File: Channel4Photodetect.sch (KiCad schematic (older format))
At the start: 5 parts

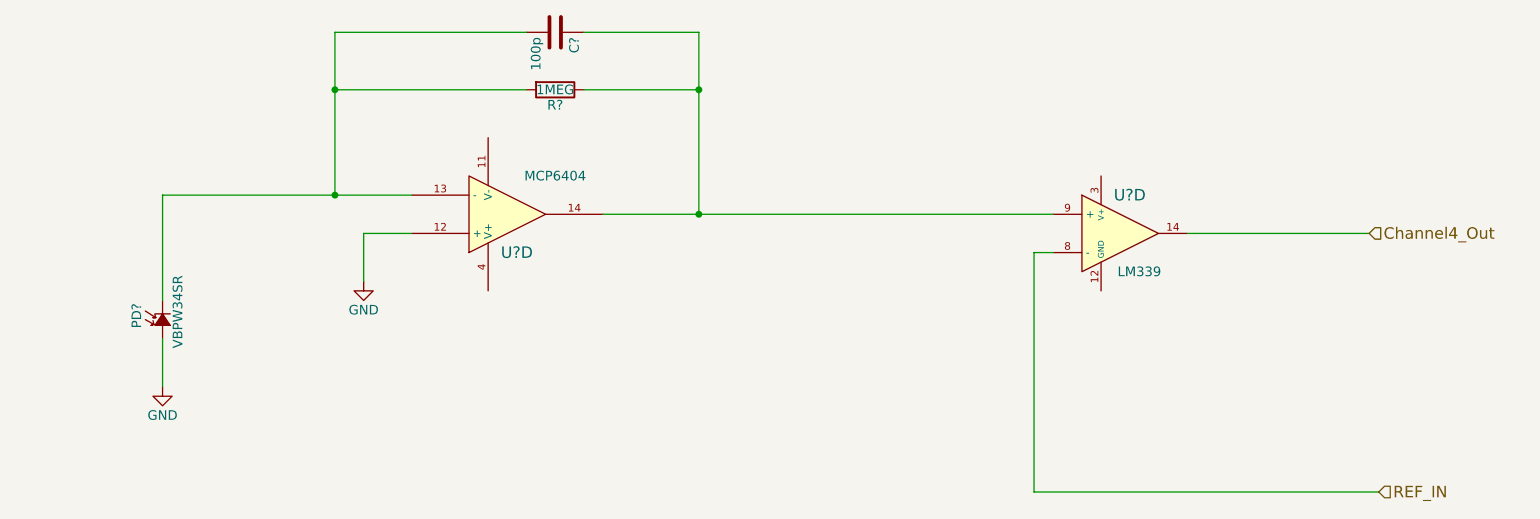
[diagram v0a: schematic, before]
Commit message: Added power regulator, VGND and test points
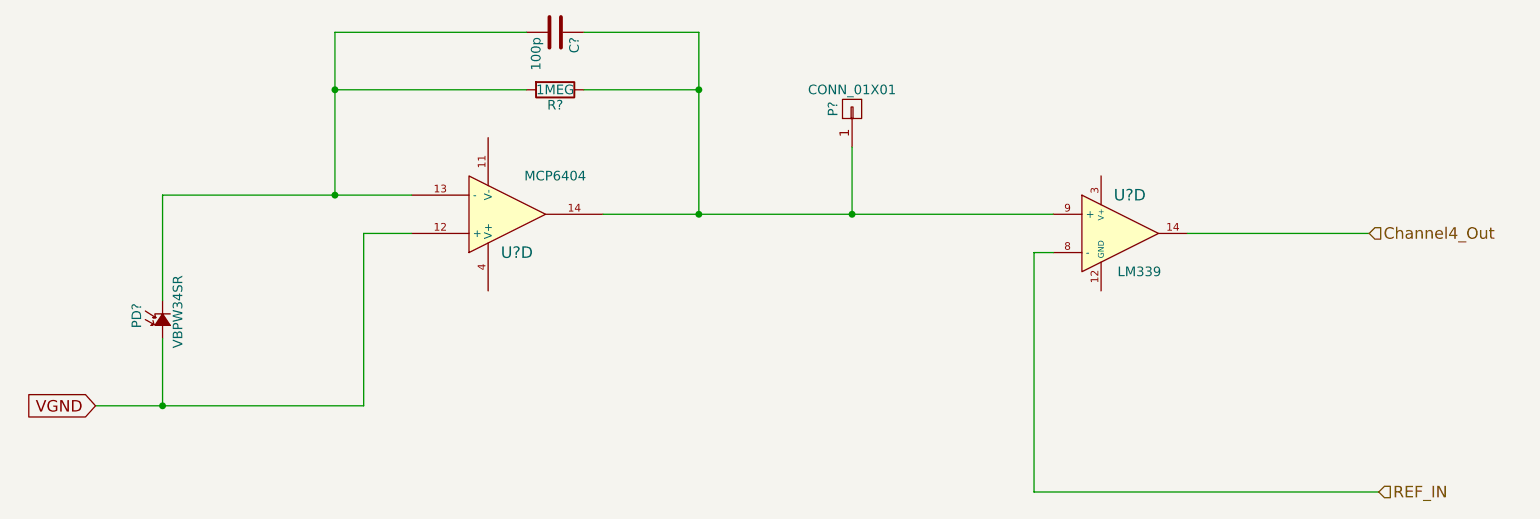
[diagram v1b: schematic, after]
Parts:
- added P?: CONN_01X01, symbol CONN_01X01
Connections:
- net at C?.1, R?.1, U?.14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: now also P?.1 (P1)
- net GND renamed VGND
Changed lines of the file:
@@
 LIBS:memory
 LIBS:xilinx
-LIBS:special
 LIBS:microcontrollers
 LIBS:dsp
@@
 	4550 2550 5150 2550
 Connection ~ 5150 2850
-$Comp
-L GND #PWR?
-U 1 1 5552FFE1
-P 3400 3850
-F 0 "#PWR?" H 3400 3600 50  0001 C CNN
-F 1 "GND" H 3400 3700 50  0000 C CNN
-F 2 "" H 3400 3850 60  0000 C CNN
-F 3 "" H 3400 3850 60  0000 C CNN
-	1    3400 3850
-	1    0    0    -1
-$EndComp
 Wire Wire Line
 	3650 3600 3400 3600
-Wire Wire Line
-	3400 3600 3400 3850
-$Comp
-L GND #PWR?
-U 1 1 5552FFFC
-P 2350 4400
-F 0 "#PWR?" H 2350 4150 50  0001 C CNN
-F 1 "GND" H 2350 4250 50  0000 C CNN
-F 2 "" H 2350 4400 60  0000 C CNN
-F 3 "" H 2350 4400 60  0000 C CNN
-	1    2350 4400
-	1    0    0    -1
-$EndComp
-Wire Wire Line
-	2350 4150 2350 4400
 $Comp
 L LM339 U?
@@
 Wire Wire Line
 	6900 4950 6900 3700
+$Comp
+L CONN_01X01 P?
+U 1 1 555633D1
+P 5950 2950
+F 0 "P?" H 5950 3050 50  0000 C CNN
+F 1 "CONN_01X01" V 6050 2950 50  0000 C CNN
+F 2 "" H 5950 2950 60  0000 C CNN
+F 3 "" H 5950 2950 60  0000 C CNN
+	1    5950 2950
+	0    -1   -1   0
+$EndComp
+Wire Wire Line
+	5950 3150 5950 3500
+Connection ~ 5950 3500
+Wire Wire Line
+	3400 4500 3400 3600
+Wire Wire Line
+	2000 4500 3400 4500
+Wire Wire Line
+	2350 4500 2350 4150
+Text GLabel 2000 4500 0    60   Input ~ 0
+VGND
+Connection ~ 2350 4500
 $EndSCHEMATC

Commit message: Added libraries and imported components into the layout
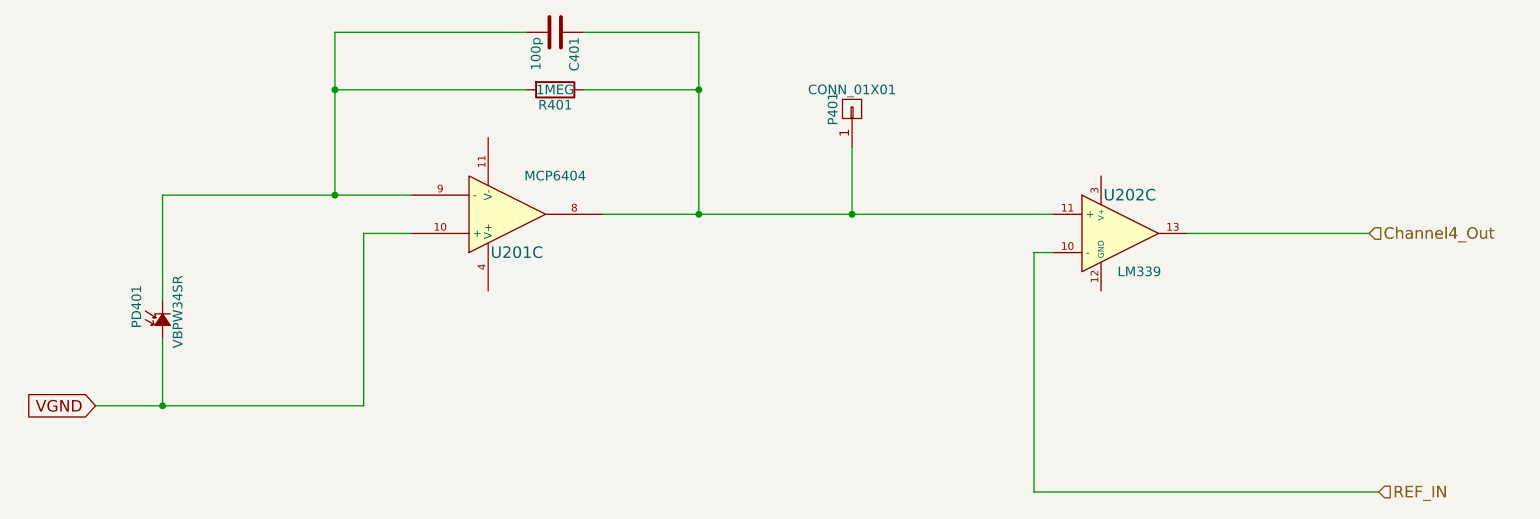
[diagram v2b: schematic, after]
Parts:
- gave numbers to parts that had none: 6
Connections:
- net Channel4_Out: now also U202.13; no longer U202.14
- net REF_IN: now also U202.10 (-); no longer U202.8 (-)
- net VGND: now also U201.10 (+); no longer U201.12 (+)
- net at C401.1, P401.1 (P1), R401.1: now also U201.8, U202.11 (+); no longer U201.14, U202.9 (+)
- net at C401.2, PD401.2 (C), R401.2: now also U201.9 (-); no longer U201.13 (-)
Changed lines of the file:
@@
 $EndDescr
 $Comp
-L R R?
+L R R401
 U 1 1 5552FFAC
 P 4400 2850
-F 0 "R?" V 4480 2850 50  0000 C CNN
+F 0 "R401" V 4480 2850 50  0000 C CNN
 F 1 "1MEG" V 4400 2850 50  0000 C CNN
 F 2 "" V 4330 2850 30  0000 C CNN
@@
 $EndComp
 $Comp
-L C C?
+L C C401
 U 1 1 5552FFB3
 P 4400 2550
-F 0 "C?" H 4425 2650 50  0000 L CNN
+F 0 "C401" H 4425 2650 50  0000 L CNN
 F 1 "100p" H 4425 2450 50  0000 L CNN
 F 2 "" H 4438 2400 30  0000 C CNN
@@
 $EndComp
 $Comp
-L MCP6404-E/SL U?
-U 4 1 5552FFBC
+L MCP6404-E/SL U201
+U 3 1 5552FFBC
 P 4150 3500
-F 0 "U?" H 4200 3700 60  0000 C CNN
+F 0 "U201" H 4200 3700 60  0000 C CNN
 F 1 "MCP6404" H 4400 3300 50  0000 C CNN
 F 2 "" H 4150 3500 60  0000 C CNN
@@
 F 4 "MCP6404-E/SL" H 4150 3500 60  0001 C CNN "MPN"
 F 5 "http://parts.io/detail/3584122/MCP6404-E%2FSL" H 4150 3500 60  0001 C CNN "Link"
-	4    4150 3500
+	3    4150 3500
 	1    0    0    1
 $EndComp
 $Comp
-L Photodiode PD?
+L Photodiode PD401
 U 1 1 5552FFC5
 P 2350 4050
-F 0 "PD?" H 2305 4185 50  0000 L CNN
+F 0 "PD401" H 2305 4185 50  0000 L CNN
 F 1 "VBPW34SR" H 2200 3970 50  0000 L CNN
 F 2 "" V 2350 4050 60  0000 C CNN
@@
 	3650 3600 3400 3600
 $Comp
-L LM339 U?
-U 4 1 55530005
+L LM339 U202
+U 3 1 55530005
 P 7350 3600
-F 0 "U?" H 7400 3800 60  0000 C CNN
+F 0 "U202" H 7400 3800 60  0000 C CNN
 F 1 "LM339" H 7450 3400 50  0000 C CNN
 F 2 "" H 7350 3600 60  0000 C CNN
@@
 F 4 "LM339DE4" H 7350 3600 60  0001 C CNN "MPN"
 F 5 "http://parts.io/detail/916254/LM339DE4" H 7350 3600 60  0001 C CNN "Link"
-	4    7350 3600
+	3    7350 3600
 	1    0    0    -1
 $EndComp
@@
 	6900 4950 6900 3700
 $Comp
-L CONN_01X01 P?
+L CONN_01X01 P401
 U 1 1 555633D1
 P 5950 2950
-F 0 "P?" H 5950 3050 50  0000 C CNN
+F 0 "P401" H 5950 3050 50  0000 C CNN
 F 1 "CONN_01X01" V 6050 2950 50  0000 C CNN
 F 2 "" H 5950 2950 60  0000 C CNN
@@
 Connection ~ 5950 3500
 Wire Wire Line
-	3400 4500 3400 3600
+	3400 3600 3400 4500
 Wire Wire Line
-	2000 4500 3400 4500
+	3400 4500 2000 4500
 Wire Wire Line
 	2350 4500 2350 4150

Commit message: Added photodiode component to new local footprint library
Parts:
- C401: footprint (none) -> Capacitors_SMD:C_0805_HandSoldering
- P401: footprint (none) -> Pin_Headers:Pin_Header_Straight_1x01
- PD401: footprint (none) -> DasBlinkinput:VPW34SR
- R401: footprint (none) -> Resistors_SMD:R_1206_HandSoldering
- U201, U202: footprint (none) -> Housings_SOIC:SOIC-14_3.9x8.7mm_Pitch1.27mm
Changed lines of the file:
@@
 F 0 "R401" V 4480 2850 50  0000 C CNN
 F 1 "1MEG" V 4400 2850 50  0000 C CNN
-F 2 "" V 4330 2850 30  0000 C CNN
+F 2 "Resistors_SMD:R_1206_HandSoldering" V 4330 2850 30  0001 C CNN
 F 3 "" H 4400 2850 30  0000 C CNN
 F 4 "RC1206FR-071ML" V 4400 2850 60  0001 C CNN "MPN"
@@
 F 0 "C401" H 4425 2650 50  0000 L CNN
 F 1 "100p" H 4425 2450 50  0000 L CNN
-F 2 "" H 4438 2400 30  0000 C CNN
+F 2 "Capacitors_SMD:C_0805_HandSoldering" H 4438 2400 30  0001 C CNN
 F 3 "" H 4400 2550 60  0000 C CNN
 	1    4400 2550
@@
 F 0 "U201" H 4200 3700 60  0000 C CNN
 F 1 "MCP6404" H 4400 3300 50  0000 C CNN
-F 2 "" H 4150 3500 60  0000 C CNN
+F 2 "Housings_SOIC:SOIC-14_3.9x8.7mm_Pitch1.27mm" H 4150 3500 60  0001 C CNN
 F 3 "" H 4150 3500 60  0000 C CNN
 F 4 "MCP6404-E/SL" H 4150 3500 60  0001 C CNN "MPN"
@@
 F 0 "PD401" H 2305 4185 50  0000 L CNN
 F 1 "VBPW34SR" H 2200 3970 50  0000 L CNN
-F 2 "" V 2350 4050 60  0000 C CNN
+F 2 "DasBlinkinput:VPW34SR" V 2350 4050 60  0001 C CNN
 F 3 "" V 2350 4050 60  0000 C CNN
 F 4 "VBPW34SR" H 2350 4050 60  0001 C CNN "MPN"
@@
 F 0 "U202" H 7400 3800 60  0000 C CNN
 F 1 "LM339" H 7450 3400 50  0000 C CNN
-F 2 "" H 7350 3600 60  0000 C CNN
+F 2 "Housings_SOIC:SOIC-14_3.9x8.7mm_Pitch1.27mm" H 7350 3600 60  0001 C CNN
 F 3 "" H 7350 3600 60  0000 C CNN
 F 4 "LM339DE4" H 7350 3600 60  0001 C CNN "MPN"
@@
 F 0 "P401" H 5950 3050 50  0000 C CNN
 F 1 "CONN_01X01" V 6050 2950 50  0000 C CNN
-F 2 "" H 5950 2950 60  0000 C CNN
+F 2 "Pin_Headers:Pin_Header_Straight_1x01" H 5950 2950 60  0001 C CNN
 F 3 "" H 5950 2950 60  0000 C CNN
 	1    5950 2950

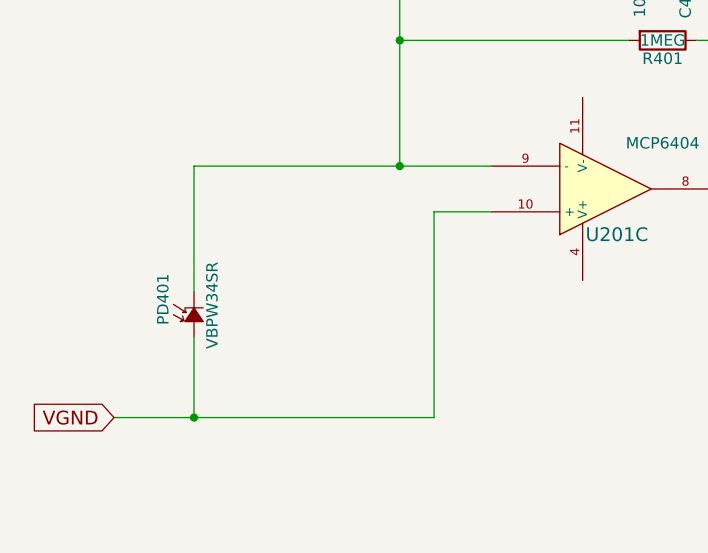
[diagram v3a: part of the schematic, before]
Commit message: Added secondary footprint for photodiode
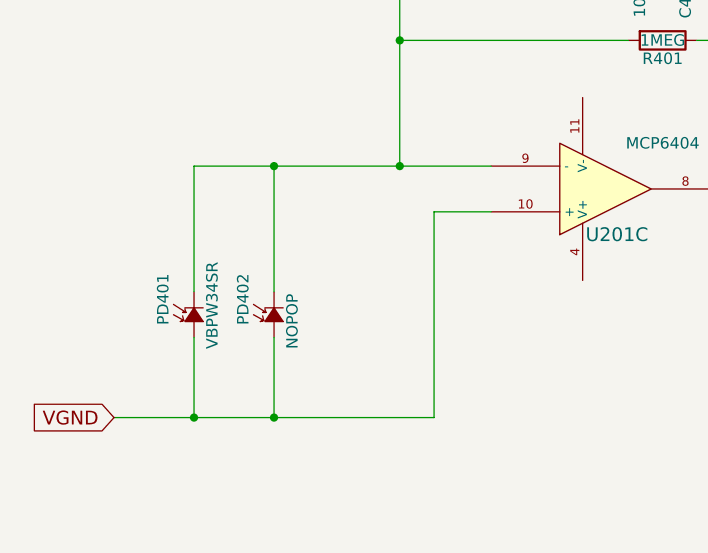
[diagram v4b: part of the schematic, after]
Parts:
- added PD402: NOPOP, Capacitors_SMD:C_0805_HandSoldering, symbol Photodiode
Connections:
- net VGND: now also PD402.1 (A)
- net at C401.2, PD401.2 (C), R401.2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: now also PD402.2 (C)
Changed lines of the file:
@@
 $EndComp
 Wire Wire Line
-	3650 3400 2350 3400
+	2350 3400 3650 3400
 Wire Wire Line
 	2350 3400 2350 3950
@@
 Connection ~ 5950 3500
 Wire Wire Line
-	3400 3600 3400 4500
+	3400 4500 3400 3600
 Wire Wire Line
-	3400 4500 2000 4500
+	2000 4500 3400 4500
 Wire Wire Line
 	2350 4500 2350 4150
@@
 VGND
 Connection ~ 2350 4500
+$Comp
+L Photodiode PD402
+U 1 1 555A3FB6
+P 2700 4050
+F 0 "PD402" H 2655 4185 50  0000 L CNN
+F 1 "NOPOP" H 2550 3970 50  0000 L CNN
+F 2 "Capacitors_SMD:C_0805_HandSoldering" V 2700 4050 60  0001 C CNN
+F 3 "" V 2700 4050 60  0000 C CNN
+F 4 "TEMD6200FX01" H 2700 4050 60  0001 C CNN "MPN"
+F 5 "http://parts.io/detail/2942502/TEMD6200FX01" H 2700 4050 60  0001 C CNN "Link"
+	1    2700 4050
+	0    -1   -1   0
+$EndComp
+Wire Wire Line
+	2700 3950 2700 3400
+Connection ~ 2700 3400
+Wire Wire Line
+	2700 4150 2700 4500
+Connection ~ 2700 4500
 $EndSCHEMATC

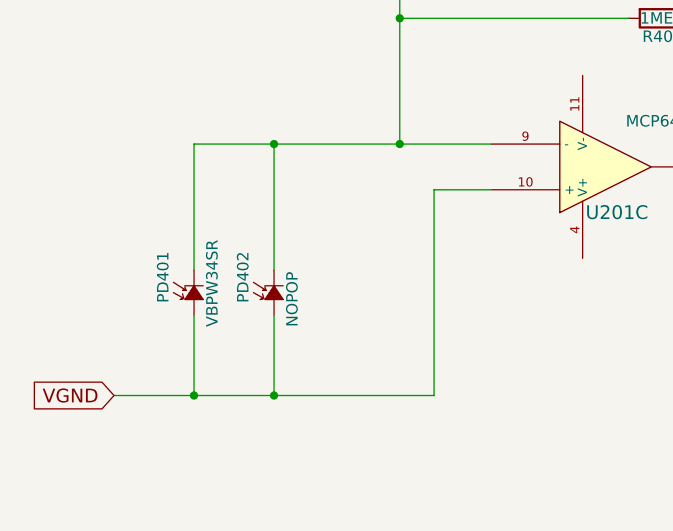
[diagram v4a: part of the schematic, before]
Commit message: Removing extra set of photodiodes and changing the original photodiode footprint
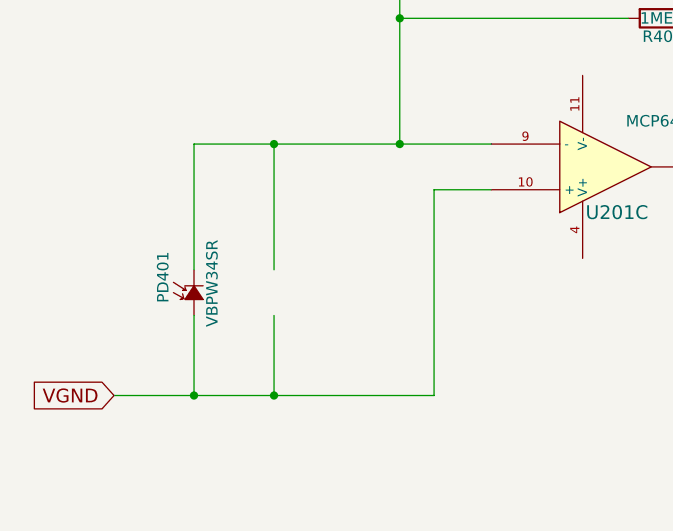
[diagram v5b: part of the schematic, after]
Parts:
- removed PD402: NOPOP, Capacitors_SMD:C_0805_HandSoldering, symbol Photodiode
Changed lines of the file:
@@
 VGND
 Connection ~ 2350 4500
-$Comp
-L Photodiode PD402
-U 1 1 555A3FB6
-P 2700 4050
-F 0 "PD402" H 2655 4185 50  0000 L CNN
-F 1 "NOPOP" H 2550 3970 50  0000 L CNN
-F 2 "Capacitors_SMD:C_0805_HandSoldering" V 2700 4050 60  0001 C CNN
-F 3 "" V 2700 4050 60  0000 C CNN
-F 4 "TEMD6200FX01" H 2700 4050 60  0001 C CNN "MPN"
-F 5 "http://parts.io/detail/2942502/TEMD6200FX01" H 2700 4050 60  0001 C CNN "Link"
-	1    2700 4050
-	0    -1   -1   0
-$EndComp
 Wire Wire Line
 	2700 3950 2700 3400

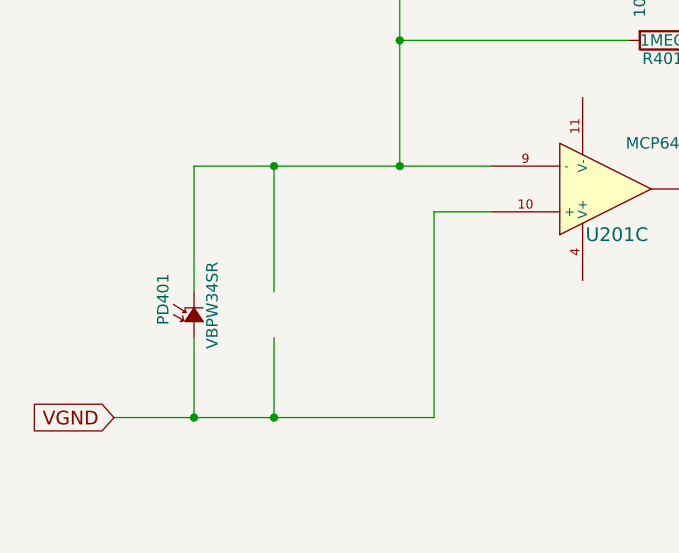
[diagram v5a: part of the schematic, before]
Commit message: Schematic and layout cleanup after photodiode removal
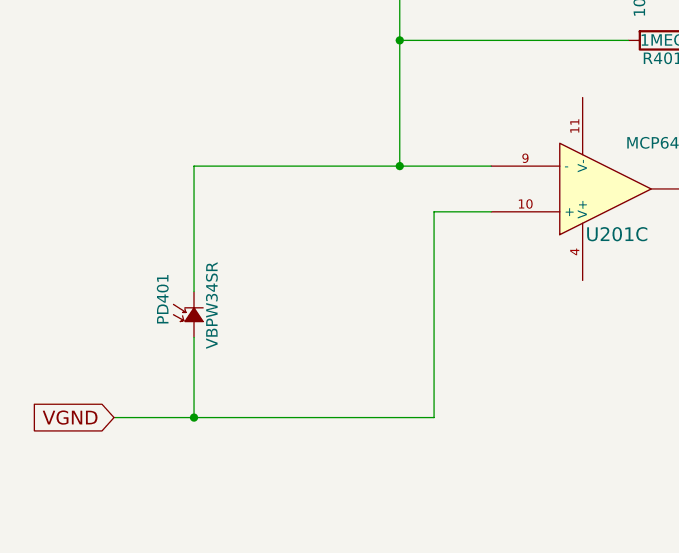
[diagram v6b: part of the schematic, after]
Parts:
- PD401: footprint DasBlinkinput:VPW34SR -> DasBlinkinput:VPW34SR*
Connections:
- wire segments 20 -> 18
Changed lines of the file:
@@
 F 0 "PD401" H 2305 4185 50  0000 L CNN
 F 1 "VBPW34SR" H 2200 3970 50  0000 L CNN
-F 2 "DasBlinkinput:VPW34SR" V 2350 4050 60  0001 C CNN
+F 2 "DasBlinkinput:VPW34SR*" V 2350 4050 60  0001 C CNN
 F 3 "" V 2350 4050 60  0000 C CNN
 F 4 "VBPW34SR" H 2350 4050 60  0001 C CNN "MPN"
@@
 Connection ~ 5950 3500
 Wire Wire Line
-	3400 4500 3400 3600
+	3400 3600 3400 4500
 Wire Wire Line
-	2000 4500 3400 4500
+	3400 4500 2000 4500
 Wire Wire Line
 	2350 4500 2350 4150
@@
 VGND
 Connection ~ 2350 4500
-Wire Wire Line
-	2700 3950 2700 3400
-Connection ~ 2700 3400
-Wire Wire Line
-	2700 4150 2700 4500
-Connection ~ 2700 4500
 $EndSCHEMATC

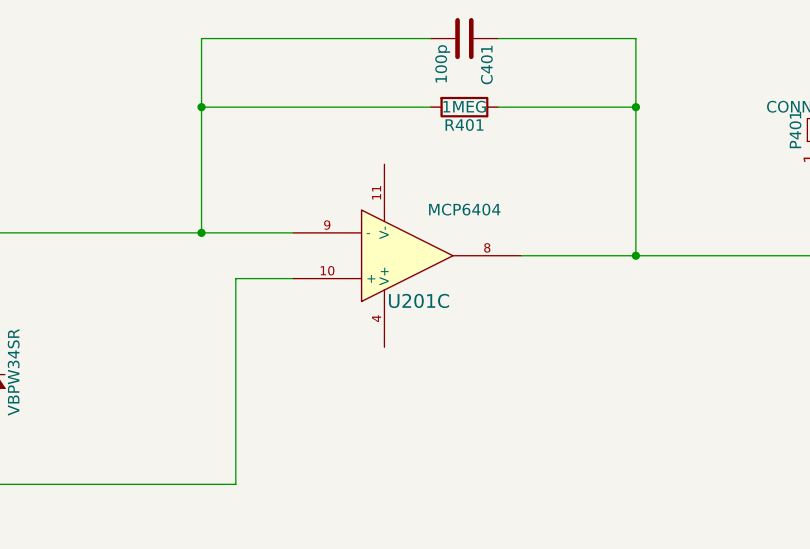
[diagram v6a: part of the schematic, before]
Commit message: Routed all passives related to U201 and the photodiodes
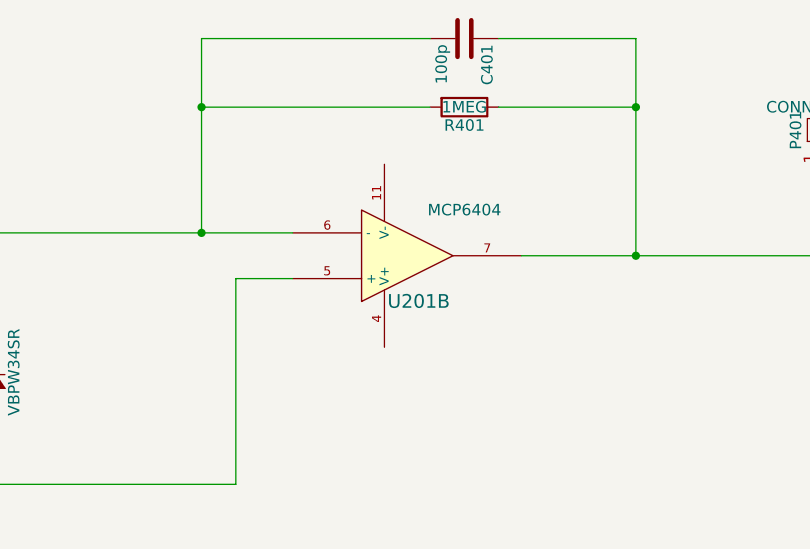
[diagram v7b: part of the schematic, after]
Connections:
- net VGND: now also U201.5 (+); no longer U201.10 (+)
- net at C401.1, P401.1 (P1), R401.1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: now also U201.7; no longer U201.8
- net at C401.2, PD401.2 (C), R401.2: now also U201.6 (-); no longer U201.9 (-)
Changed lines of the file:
@@
 $Comp
 L MCP6404-E/SL U201
-U 3 1 5552FFBC
+U 2 1 5552FFBC
 P 4150 3500
 F 0 "U201" H 4200 3700 60  0000 C CNN
@@
 F 4 "MCP6404-E/SL" H 4150 3500 60  0001 C CNN "MPN"
 F 5 "http://parts.io/detail/3584122/MCP6404-E%2FSL" H 4150 3500 60  0001 C CNN "Link"
-	3    4150 3500
+	2    4150 3500
 	1    0    0    1
 $EndComp

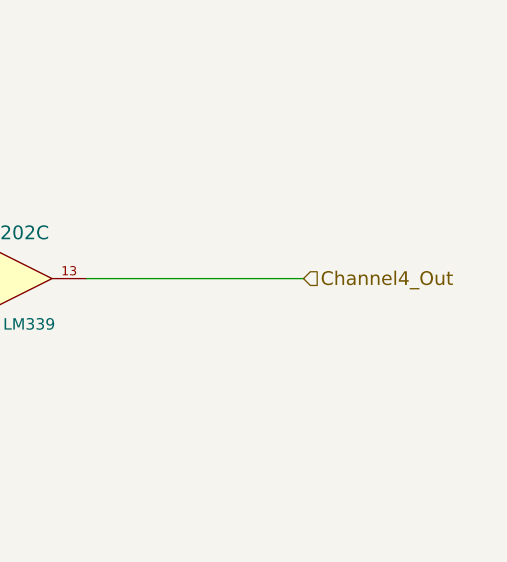
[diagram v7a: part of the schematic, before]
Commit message: Routed remainder of lines and added test points with lables
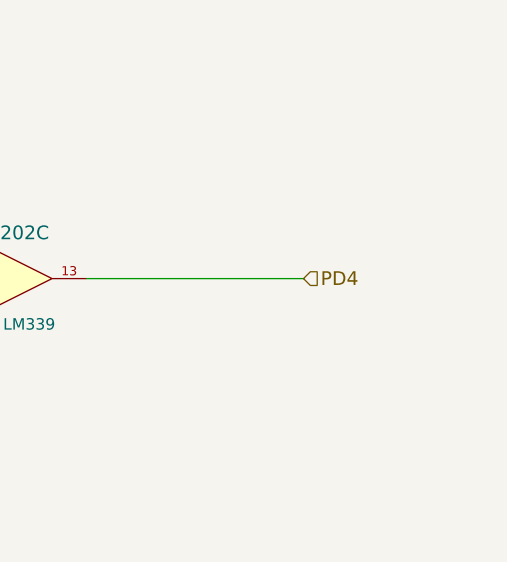
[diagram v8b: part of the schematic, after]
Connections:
- net Channel4_Out renamed PD4
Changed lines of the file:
@@
 	7700 3600 8650 3600
 Text HLabel 8650 3600 2    60   Input ~ 0
-Channel4_Out
+PD4
 Text HLabel 8700 4950 2    60   Input ~ 0
 REF_IN
